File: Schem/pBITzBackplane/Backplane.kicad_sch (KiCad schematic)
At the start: 32 parts, among them J2 pBITzBus, J3 pBITzBus, J4 pBITzBus, J5 pBITzBus, J6 FH69-60S-0.5SH, J7 FH69-60S-0.5SH

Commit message: Added all the manufacturer part numbers to the KiCad schematics and PCB files. This will make it easier to order the parts for the project and ensure that the correct components are used. I also removed some of the old schematics that were no longer needed, such as the BaudClock, ConsolePort, DeviceSelectDecode, GPIOUserSerial, IO Controller, UserPorts, Video, and Z80HomeBrew schematics. These changes will help to streamline the design and make it easier to understand.
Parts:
- R10, R11, R12, R13, R14, R15, R16, R17, R6, R7, R9: MANUFACTURER_PART_NUMBER (none) -> RC0603FR-074K7L
- RN1, RN2: MANUFACTURER_PART_NUMBER (none) -> 4820P-2-472LF
- RN10, RN11, RN12, RN13, RN14, RN15, RN4, RN5, RN6, RN7, RN8, RN9: MANUFACTURER_PART_NUMBER (none) -> EXB-2HV330JV
- RN3: MANUFACTURER_PART_NUMBER (none) -> 4816P-T02-472LF
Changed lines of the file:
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@@
 			)
 		)
+		(property "MANUFACTURER_PART_NUMBER" "RC0603FR-074K7L"
+			(at 207.01 194.31 90)
+			(effects
+				(font
+					(size 1.27 1.27)
+				)
+				(hide yes)
+			)
+		)
 		(pin "1"
 		)
@@
 			)
 		)
+		(property "MANUFACTURER_PART_NUMBER" "EXB-2HV330JV"
+			(at 521.97 378.46 0)
+			(effects
+				(font
+					(size 1.27 1.27)
+				)
+				(hide yes)
+			)
+		)
 		(pin "7"
 		)
@@
 			)
 		)
+		(property "MANUFACTURER_PART_NUMBER" "EXB-2HV330JV"
+			(at 521.97 346.71 0)
+			(effects
+				(font
+					(size 1.27 1.27)
+				)
+				(hide yes)
+			)
+		)
 		(pin "7"
 		)
@@
 			)
 		)
+		(property "MANUFACTURER_PART_NUMBER" "4816P-T02-472LF"
+			(at 143.51 218.44 0)
+			(effects
+				(font
+					(size 1.27 1.27)
+				)
+				(hide yes)
+			)
+		)
 		(pin "14"
 		)
@@
 			)
 		)
+		(property "MANUFACTURER_PART_NUMBER" "RC0603FR-074K7L"
+			(at 160.02 194.31 90)
+			(effects
+				(font
+					(size 1.27 1.27)
+				)
+				(hide yes)
+			)
+		)
 		(pin "1"
 		)
@@
 			)
 		)
+		(property "MANUFACTURER_PART_NUMBER" "EXB-2HV330JV"
+			(at 612.14 314.96 0)
+			(effects
+				(font
+					(size 1.27 1.27)
+				)
+				(hide yes)
+			)
+		)
 		(pin "7"
 		)
@@
 			)
 		)
+		(property "MANUFACTURER_PART_NUMBER" "4820P-2-472LF"
+			(at 83.82 173.99 0)
+			(effects
+				(font
+					(size 1.27 1.27)
+				)
+				(hide yes)
+			)
+		)
 		(pin "12"
 		)
@@
 			)
 		)
+		(property "MANUFACTURER_PART_NUMBER" "EXB-2HV330JV"
+			(at 612.14 410.21 0)
+			(effects
+				(font
+					(size 1.27 1.27)
+				)
+				(hide yes)
+			)
+		)
 		(pin "7"
 		)
@@
 			)
 		)
+		(property "MANUFACTURER_PART_NUMBER" "RC0603FR-074K7L"
+			(at 229.87 176.53 90)
+			(effects
+				(font
+					(size 1.27 1.27)
+				)
+				(hide yes)
+			)
+		)
 		(pin "1"
 		)
@@
 			)
 		)
+		(property "MANUFACTURER_PART_NUMBER" "RC0603FR-074K7L"
+			(at 229.87 185.42 90)
+			(effects
+				(font
+					(size 1.27 1.27)
+				)
+				(hide yes)
+			)
+		)
 		(pin "1"
 		)
@@
 			)
 		)
+		(property "MANUFACTURER_PART_NUMBER" "RC0603FR-074K7L"
+			(at 207.01 176.53 90)
+			(effects
+				(font
+					(size 1.27 1.27)
+				)
+				(hide yes)
+			)
+		)
 		(pin "1"
 		)
@@
 			)
 		)
+		(property "MANUFACTURER_PART_NUMBER" "EXB-2HV330JV"
+			(at 521.97 281.94 0)
+			(effects
+				(font
+					(size 1.27 1.27)
+				)
+				(hide yes)
+			)
+		)
 		(pin "7"
 		)
@@
 			)
 		)
+		(property "MANUFACTURER_PART_NUMBER" "EXB-2HV330JV"
+			(at 521.97 314.96 0)
+			(effects
+				(font
+					(size 1.27 1.27)
+				)
+				(hide yes)
+			)
+		)
 		(pin "7"
 		)
@@
 			)
 		)
+		(property "MANUFACTURER_PART_NUMBER" "EXB-2HV330JV"
+			(at 521.97 410.21 0)
+			(effects
+				(font
+					(size 1.27 1.27)
+				)
+				(hide yes)
+			)
+		)
 		(pin "7"
 		)
@@
 			)
 		)
+		(property "MANUFACTURER_PART_NUMBER" "EXB-2HV330JV"
+			(at 612.14 378.46 0)
+			(effects
+				(font
+					(size 1.27 1.27)
+				)
+				(hide yes)
+			)
+		)
 		(pin "7"
 		)
@@
 			)
 		)
+		(property "MANUFACTURER_PART_NUMBER" "EXB-2HV330JV"
+			(at 521.97 444.5 0)
+			(effects
+				(font
+					(size 1.27 1.27)
+				)
+				(hide yes)
+			)
+		)
 		(pin "7"
 		)
@@
 			)
 		)
+		(property "MANUFACTURER_PART_NUMBER" "EXB-2HV330JV"
+			(at 612.14 346.71 0)
+			(effects
+				(font
+					(size 1.27 1.27)
+				)
+				(hide yes)
+			)
+		)
 		(pin "7"
 		)
@@
 			)
 		)
+		(property "MANUFACTURER_PART_NUMBER" "4820P-2-472LF"
+			(at 83.82 214.63 0)
+			(effects
+				(font
+					(size 1.27 1.27)
+				)
+				(hide yes)
+			)
+		)
 		(pin "12"
 		)
@@
 			)
 		)
+		(property "MANUFACTURER_PART_NUMBER" "RC0603FR-074K7L"
+			(at 160.02 185.42 90)
+			(effects
+				(font
+					(size 1.27 1.27)
+				)
+				(hide yes)
+			)
+		)
 		(pin "1"
 		)
@@
 			)
 		)
+		(property "MANUFACTURER_PART_NUMBER" "RC0603FR-074K7L"
+			(at 184.15 194.31 90)
+			(effects
+				(font
+					(size 1.27 1.27)
+				)
+				(hide yes)
+			)
+		)
 		(pin "1"
 		)
@@
 			)
 		)
+		(property "MANUFACTURER_PART_NUMBER" "RC0603FR-074K7L"
+			(at 184.15 176.53 90)
+			(effects
+				(font
+					(size 1.27 1.27)
+				)
+				(hide yes)
+			)
+		)
 		(pin "1"
 		)
@@
 			)
 		)
+		(property "MANUFACTURER_PART_NUMBER" "RC0603FR-074K7L"
+			(at 207.01 185.42 90)
+			(effects
+				(font
+					(size 1.27 1.27)
+				)
+				(hide yes)
+			)
+		)
 		(pin "1"
 		)
@@
 			)
 		)
+		(property "MANUFACTURER_PART_NUMBER" "EXB-2HV330JV"
+			(at 612.14 281.94 0)
+			(effects
+				(font
+					(size 1.27 1.27)
+				)
+				(hide yes)
+			)
+		)
 		(pin "7"
 		)
@@
 			)
 		)
+		(property "MANUFACTURER_PART_NUMBER" "RC0603FR-074K7L"
+			(at 160.02 176.53 90)
+			(effects
+				(font
+					(size 1.27 1.27)
+				)
+				(hide yes)
+			)
+		)
 		(pin "1"
 		)
@@
 			)
 		)
+		(property "MANUFACTURER_PART_NUMBER" "EXB-2HV330JV"
+			(at 612.14 444.5 0)
+			(effects
+				(font
+					(size 1.27 1.27)
+				)
+				(hide yes)
+			)
+		)
 		(pin "7"
 		)
@@
 			(at 184.15 185.42 90)
 			(effects
+				(font
+					(size 1.27 1.27)
+				)
+				(hide yes)
+			)
+		)
+		(property "MANUFACTURER_PART_NUMBER" "RC0603FR-074K7L"
+			(at 184.15 185.42 90)
+			(effects

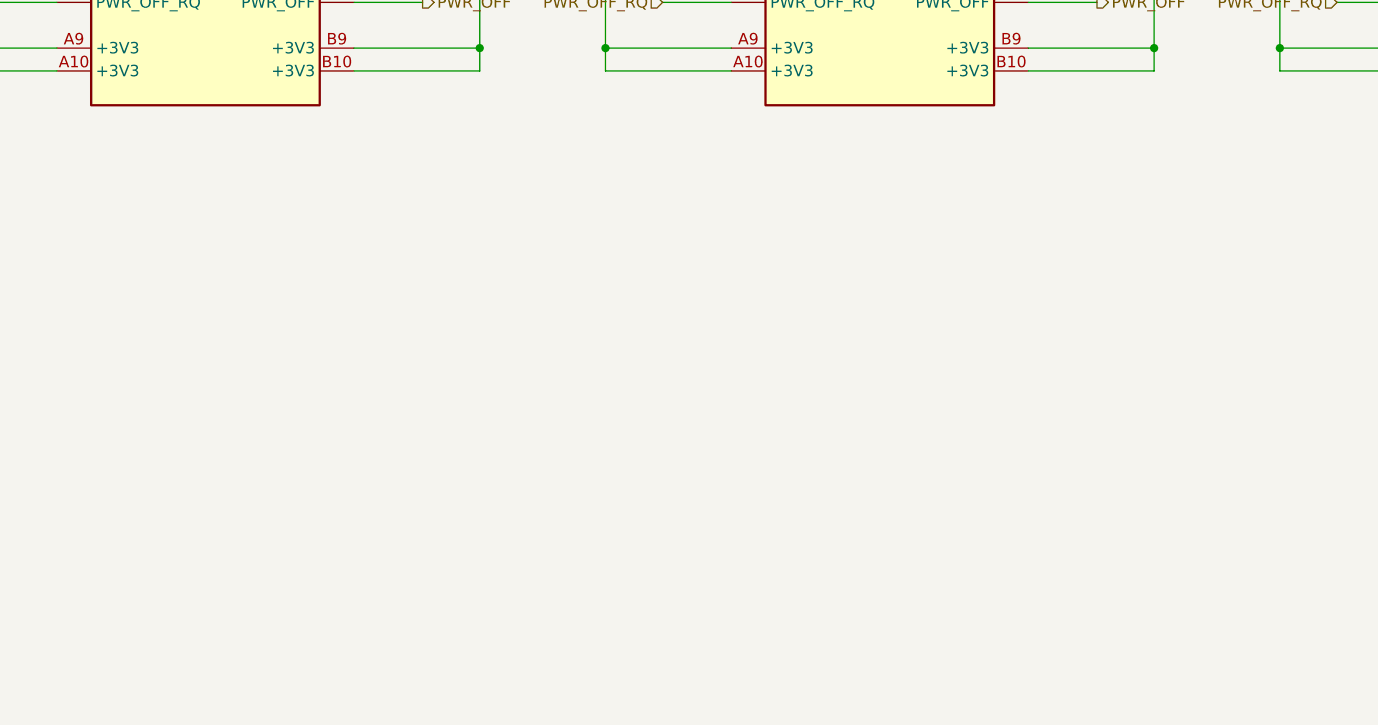
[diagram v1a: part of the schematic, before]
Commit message: Added bypass caps on power lines.
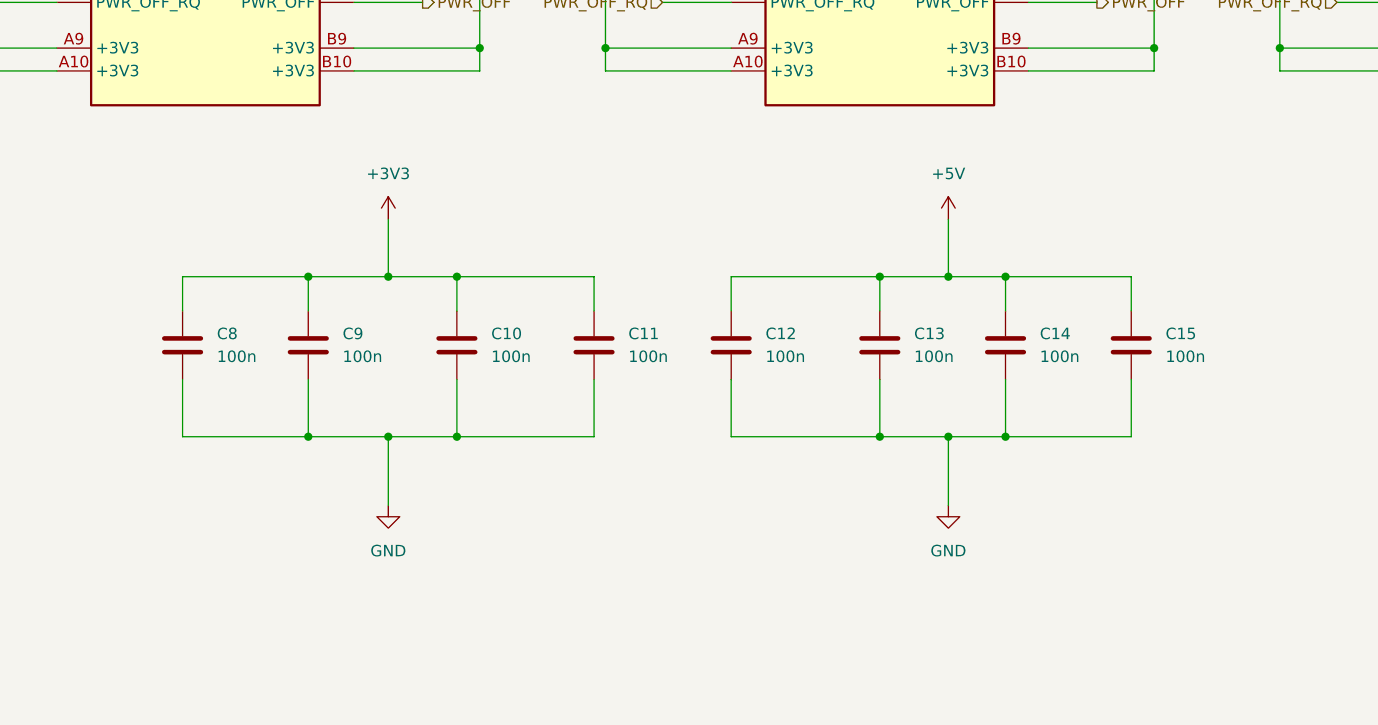
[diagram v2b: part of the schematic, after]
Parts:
- added C10, C11, C12, C13, C14, C15, C8, C9: 100n, Capacitor_SMD:C_0603_1608Metric, symbol Device:C
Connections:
- net +3V3: now also C10.1, C11.1, C8.1, C9.1
- net +5V: now also C12.1, C13.1, C14.1, C15.1
- net GND: now also C10.2, C11.2, C12.2, C13.2, C14.2, C15.2, C8.2, C9.2
